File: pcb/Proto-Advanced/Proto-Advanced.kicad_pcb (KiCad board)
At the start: 2 copper layers, 52 x 63 mm, 1145 parts, among them J1 Conn_01x04, J10 Conn_01x01, J11 Conn_01x01, J12 Conn_01x01, J13 Conn_01x01, J14 Conn_01x01, J2 Conn_01x01, J3 Conn_01x01, J4 Conn_01x01, J41 Conn_01x01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

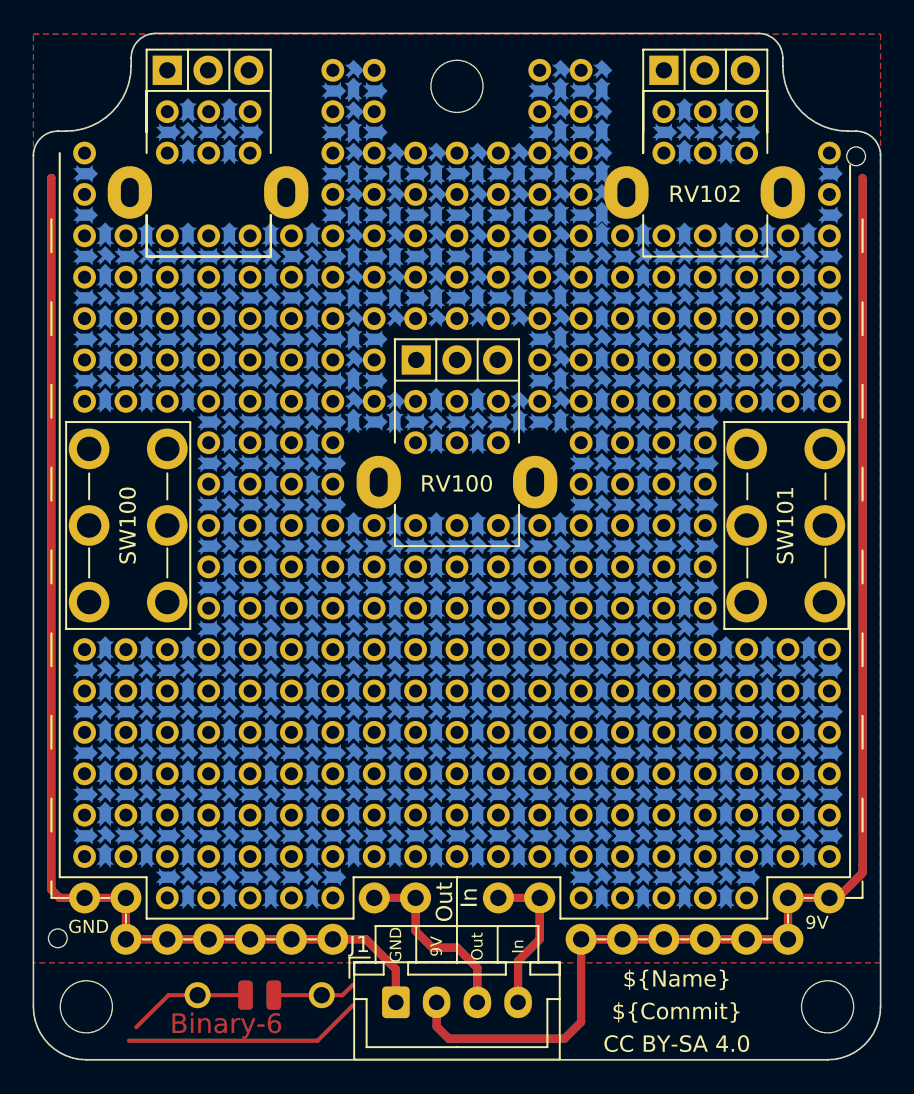
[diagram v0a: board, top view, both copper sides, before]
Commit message: [ProtoAdvanced] Update proto footprints with new tolerances
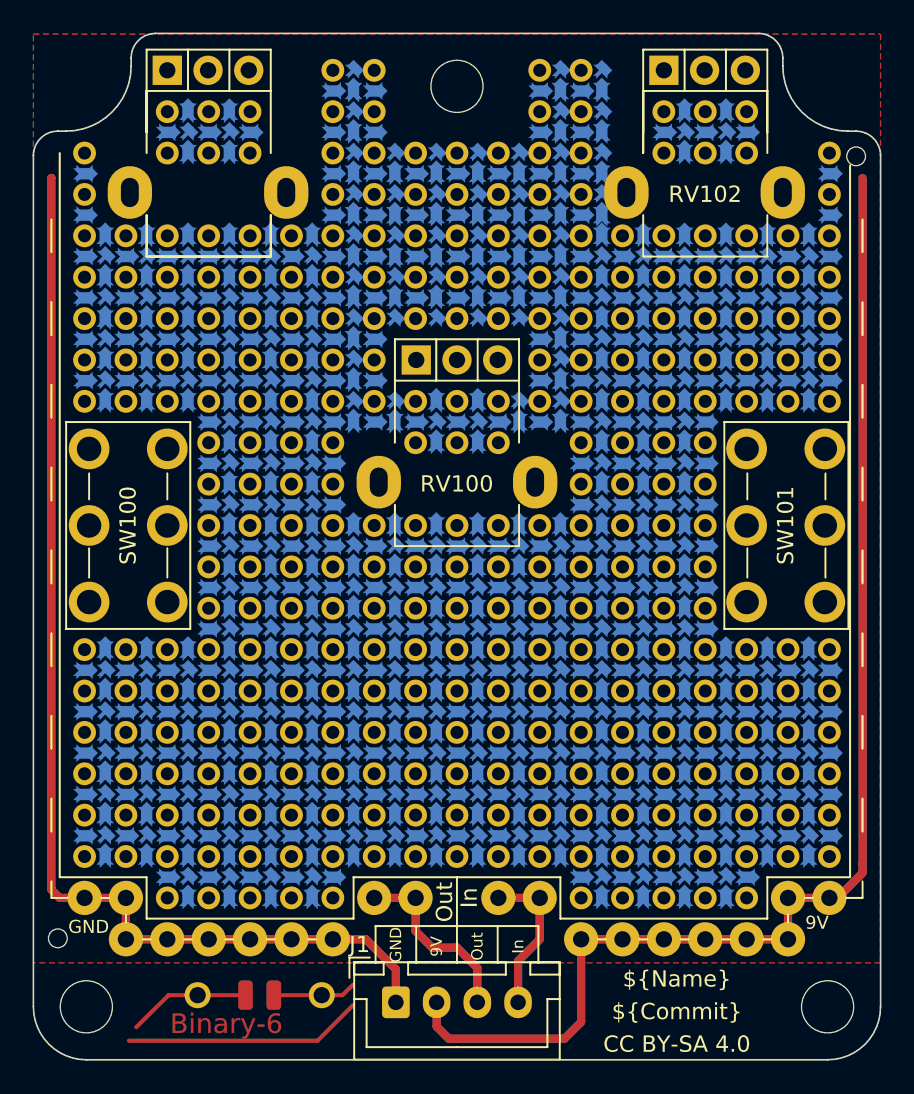
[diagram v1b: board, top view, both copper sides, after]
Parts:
- REF** (x250): footprint modules:center-pad-spikes-oneside -> MeineBib:Proto_Advanced_Shortspike
- REF** (x551): footprint modules:pad-between-spiked-oneside -> MeineBib:Proto_Advanced_Longspike
- REF** (x312): footprint modules:tht-0.8-thin-bottom -> MeineBib:Proto_Advanced_Pin_Gndplane

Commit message: [ProtoAdvanced][ProtoSimple] Make power rails wider
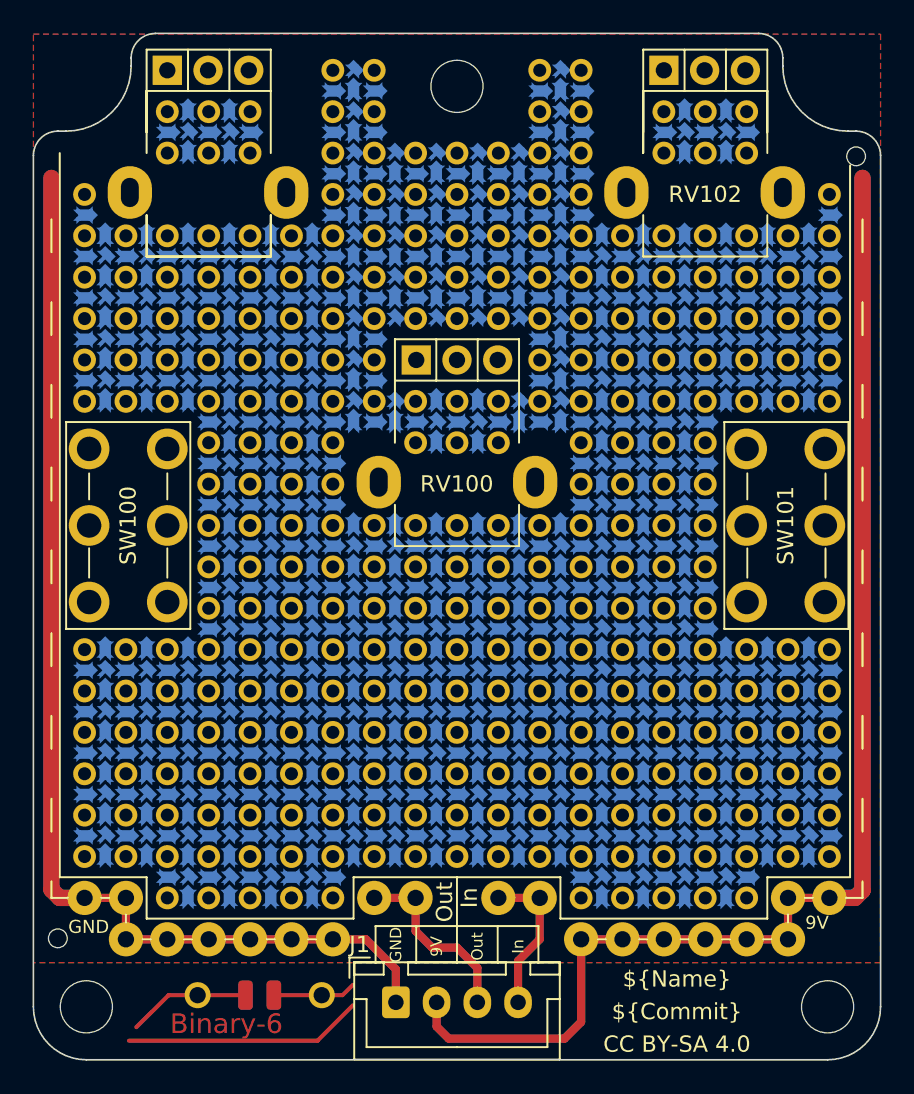
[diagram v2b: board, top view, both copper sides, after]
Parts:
- removed the REF** at (158.4, 73.6)
- removed the REF** at (158.4, 76.1)
- removed the REF** at (158.4, 71.0)
- removed the REF** at (126.6, 76.1)
- removed the REF** at (158.4, 72.3)
- removed the REF** at (172.4, 76.1)
- removed the REF** at (158.4, 74.8)
- removed the REF** at (172.4, 74.8)
- removed the REF** at (158.4, 69.8)
- removed the REF** at (158.4, 77.4)
- removed the REF** at (158.4, 78.7)
- removed the REF** at (126.6, 74.8)
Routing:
- net +9V: track 158.6 -> 159.8 mm

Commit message: [All] Update all pot footprints and silkscreens
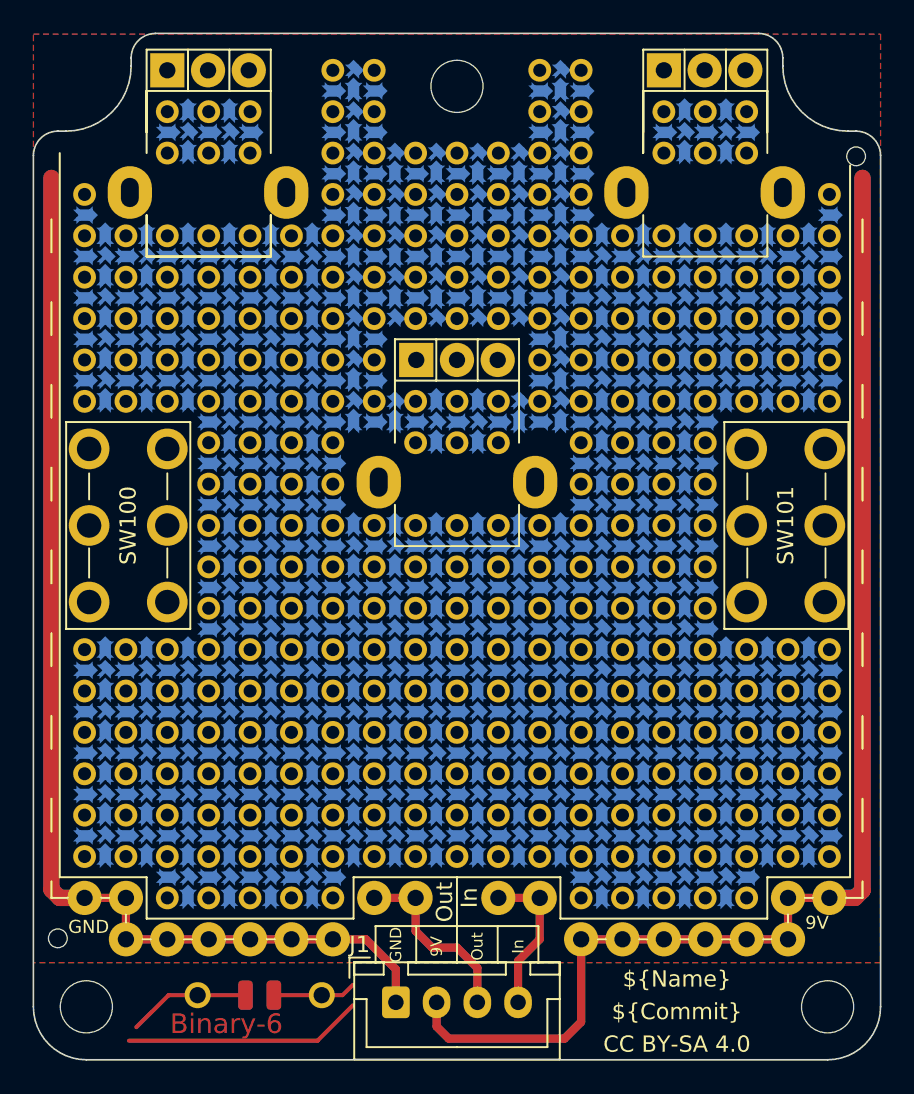
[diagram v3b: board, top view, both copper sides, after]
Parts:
- RV100, RV101, RV102: footprint Potentiometer_THT:Potentiometer_Alpha_RD901F-40-00D_Single_Vertical -> MeineBib:Potentiometer_Alpha_RD901F-40-00D_Single_Vertical

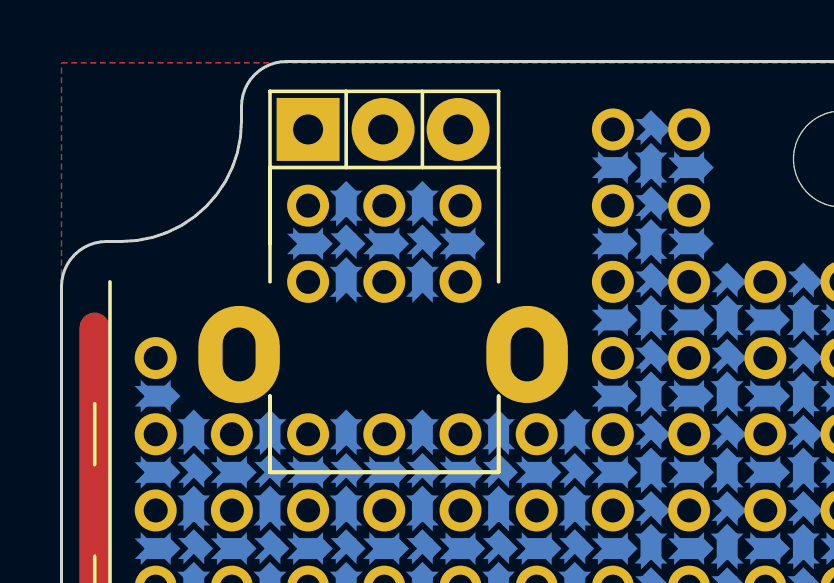
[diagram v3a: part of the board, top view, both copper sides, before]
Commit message: [All] Find out that the upper left pot is 0,08mm off on all designs
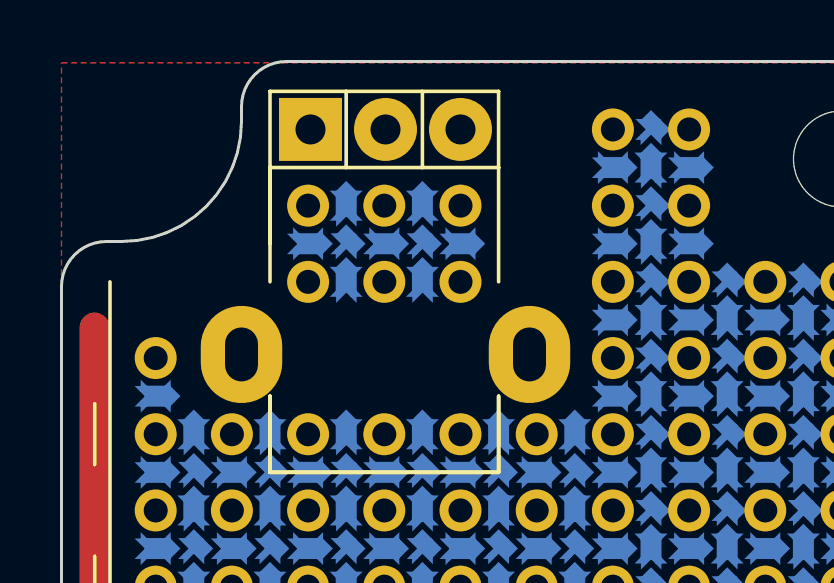
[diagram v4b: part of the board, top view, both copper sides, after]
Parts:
- moved RV101 0.08 mm to (131.8, 69.8)
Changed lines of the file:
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@@
   )
   (footprint "MeineBib:Potentiometer_Alpha_RD901F-40-00D_Single_Vertical" (layer "B.Cu")
-    (at 131.72 69.765 -90)
+    (at 131.8 69.765 -90)
     (descr "Potentiometer, vertical, 9mm, single, http://www.taiwanalpha.com.tw/downloads?target=products&id=113")
     (tags "potentiometer vertical 9mm single")
